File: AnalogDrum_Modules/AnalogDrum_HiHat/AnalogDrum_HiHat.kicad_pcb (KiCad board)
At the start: 2 copper layers, 100.3 x 160 mm, 103 parts, among them J101 Conn_01x05_Male, Q301 2N3904, Q302 2N3904, SW201 SW_DPDT_x2, SW202 SW_DPDT_x2, U201 TL074, U301 NE5532, U401 NE5532, U402 NE5532, U501 LM13700, U502 NE5532

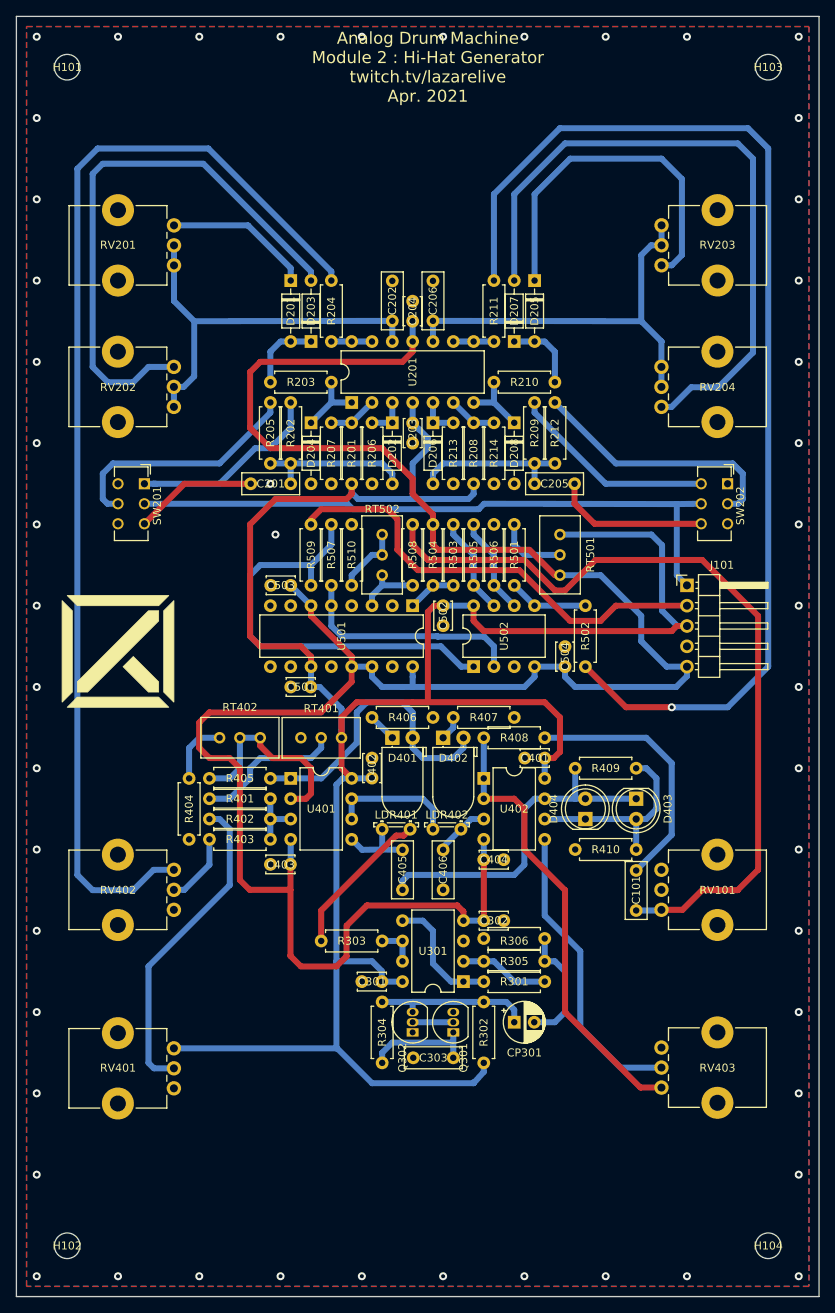
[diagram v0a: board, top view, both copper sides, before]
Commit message: Version 0.1.1
Corrections mineures :
- Vérification des potentiomètres
- Passage des connecteurs de carte e n JST
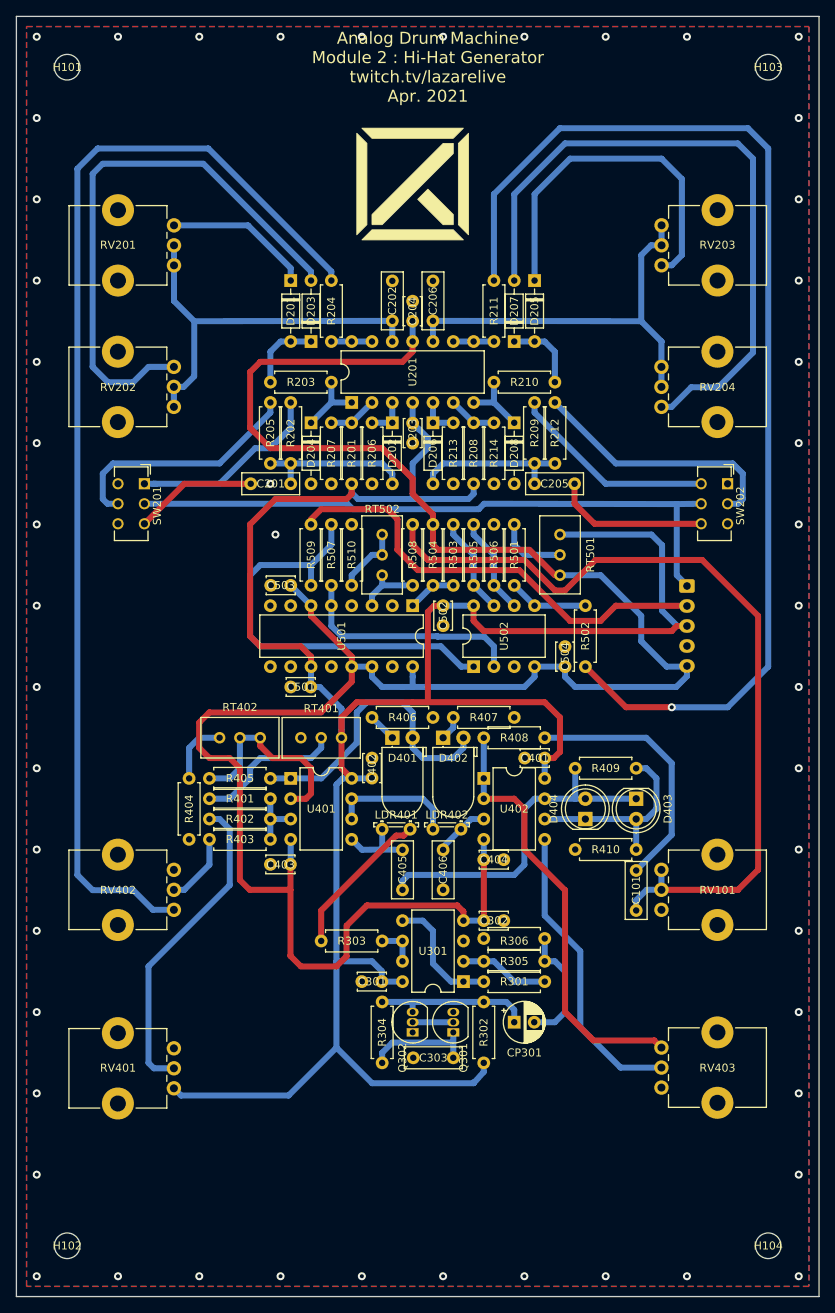
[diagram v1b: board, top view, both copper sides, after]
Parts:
- J101: footprint Connector_PinHeader_2.54mm:PinHeader_1x05_P2.54mm_Horizontal -> Connector_JST:JST_EH_B5B-EH-A_1x05_P2.50mm_Vertical; moved to B.Cu
- moved REF** 69.1 mm to (99.1, 43.8)
- moved J101 0.08 mm to (133.3, 94.1), turned to 270 degrees
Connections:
- RV101 pad 1: /VCA/SIG_IN -> GNDA
- RV101 pad 2: GNDA -> /VCA/SIG_IN
- RV101 pad 3: GNDA -> /VCA/SIG_IN
- RV401 pad 1: +12V -> GNDA
- RV401 pad 3: GNDA -> +12V
- RV402 pad 1: /EG/EGA_OUT -> GNDA
- RV402 pad 3: GNDA -> /EG/EGA_OUT
- RV403 pad 1: Net-(R408-Pad2) -> GNDA
- RV403 pad 3: GNDA -> Net-(R408-Pad2)
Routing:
- net /VCA/SIG_IN: track 101.7 -> 104.9 mm
- net +12V: track 291.0 -> 293.9 mm
- net Net-(R408-Pad2): track 56.7 -> 54.6 mm
